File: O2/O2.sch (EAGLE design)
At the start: 29 parts, among them J1 HEAD15-NOSS, J2 HEAD15-NOSS-1, J3 HEAD15-NOSS, J4 HEAD15-NOSS-1, T1 2N2222, T2 2N2222, T3 2N2222

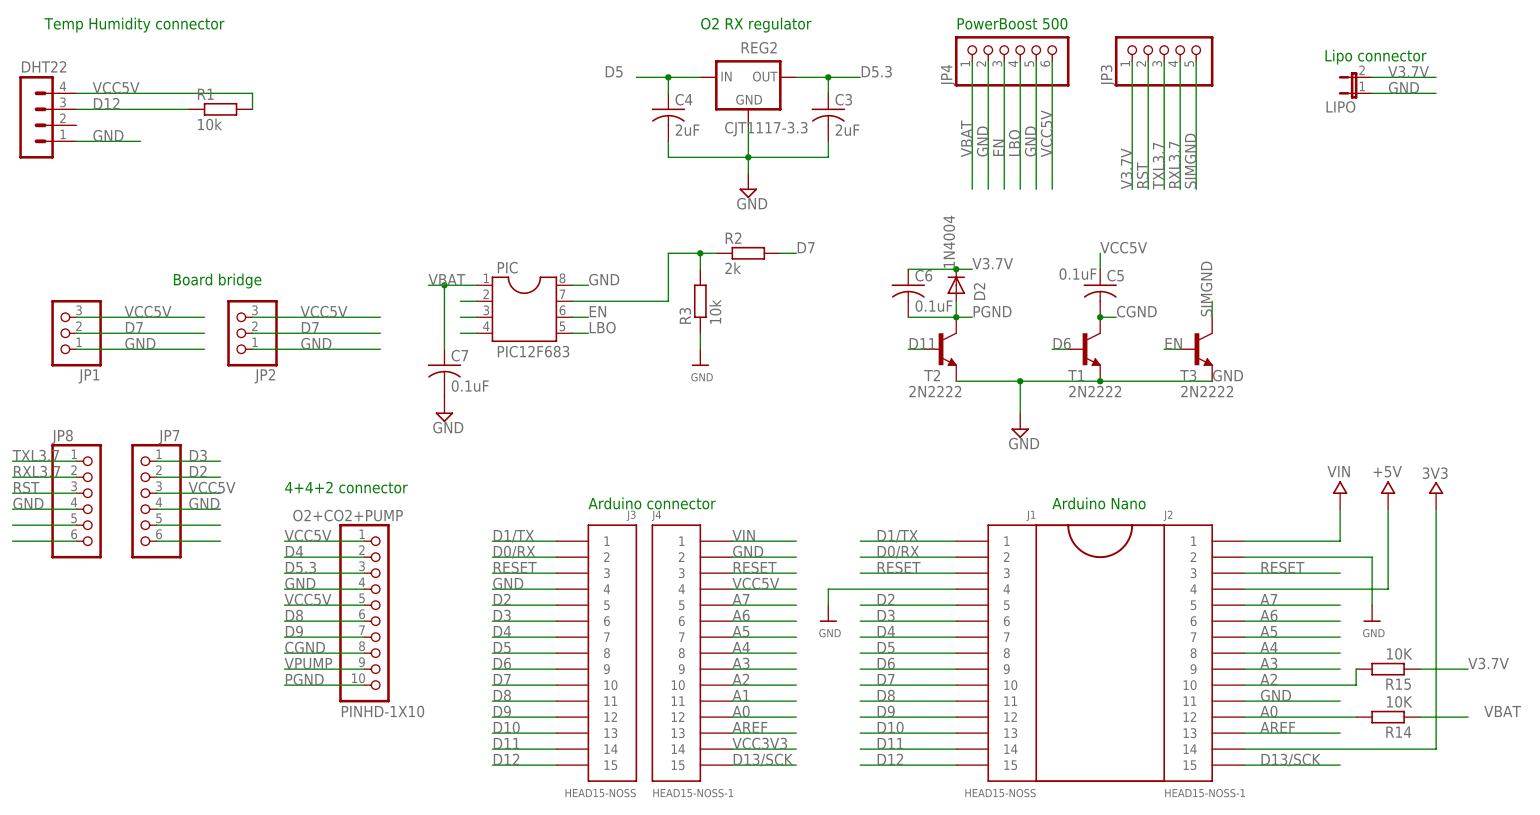
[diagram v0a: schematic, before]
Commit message: Modified the O2 circuits and changed the layout.
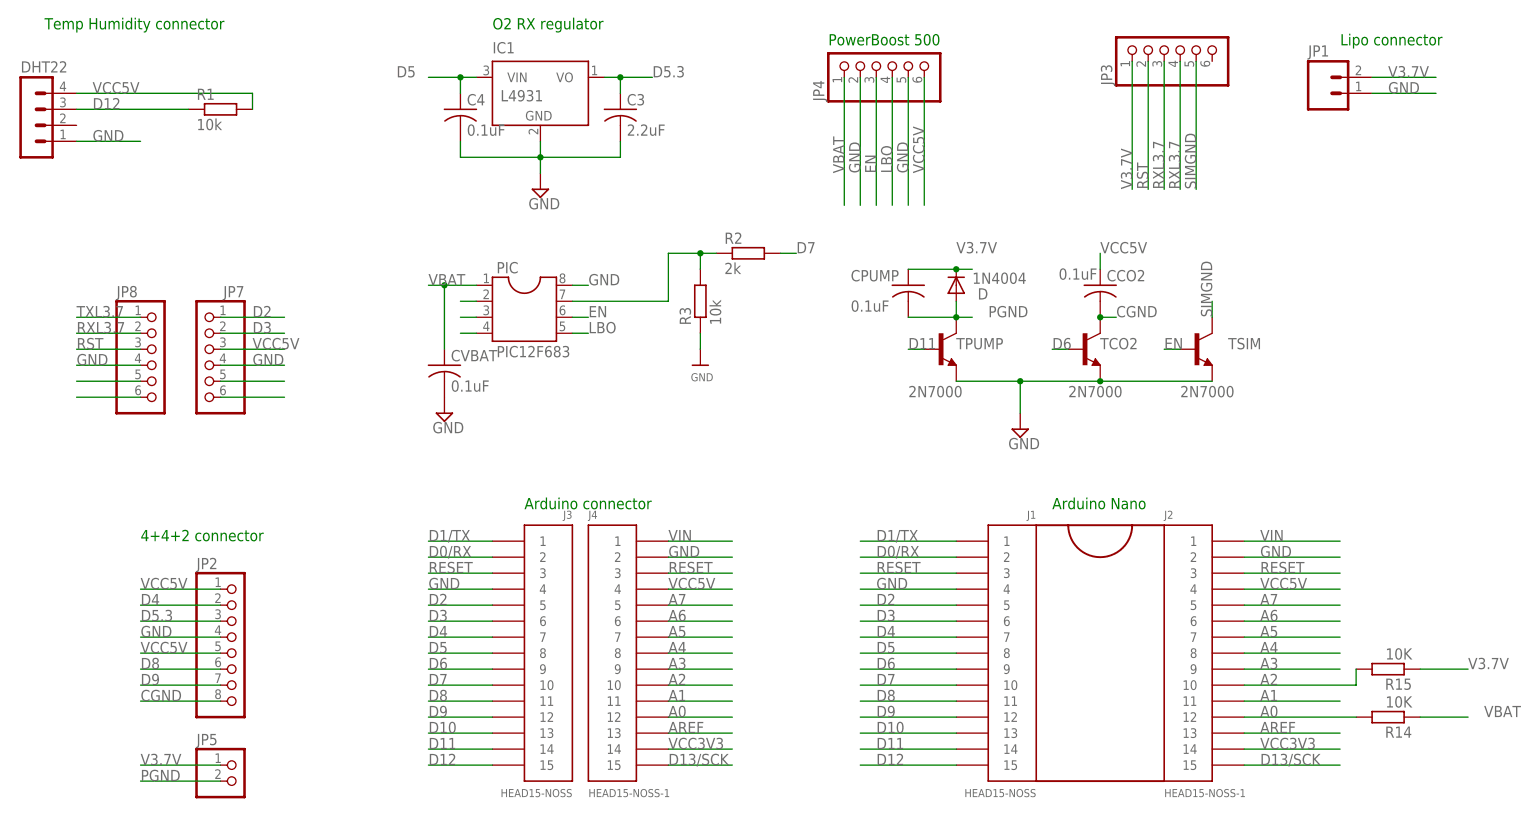
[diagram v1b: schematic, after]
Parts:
- removed LIPO: (no value), jumper:JP1E
- removed O2+CO2+PUMP: PINHD-1X10, adafruit:PINHD-1X10
- removed REG2: CJT1117-3.3, adafruit:MCP1700INLINE
- added IC1: L4931, national-semiconductor:LM2936Z-3.3
- added JP5: (no value), pinhead:PINHD-1X2
- C3: value 2uF -> 2.2uF
- C4: value 2uF -> 0.1uF
- JP1: device adafruit:PINHD-1X3CB -> SparkFun-Connectors:M023.5MM
- JP2: device adafruit:PINHD-1X3CB -> adafruit:PINHD-1X8BIG
- JP3: device pinhead:PINHD-1X55X2MM -> adafruit:PINHD-1X6CB
- TCO2, TPUMP, TSIM: value 2N2222 -> 2N7000
- renumbered C5 to CCO2, C6 to CPUMP, C7 to CVBAT, D2 to D, T1 to TCO2, T2 to TPUMP, T3 to TSIM
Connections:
- removed net VPUMP: O2+CO2+PUMP.9
- net A1: now also J2.11
- net CGND: now also JP2.8; no longer O2+CO2+PUMP.8
- net D11: now also TPUMP.B
- net D2: now also JP7.1; no longer JP7.2
- net D3: now also JP7.2; no longer JP7.1
- net D4: now also JP2.2; no longer O2+CO2+PUMP.2
- net D5: now also IC1.VIN; no longer REG2.IN
- net D5.3: now also IC1.VO, JP2.3; no longer O2+CO2+PUMP.3, REG2.OUT
- net D6: now also TCO2.B
- net D7: no longer JP1.2, JP2.2
- net D8: now also JP2.6; no longer O2+CO2+PUMP.6
- net D9: now also JP2.7; no longer O2+CO2+PUMP.7
- net GND: now also IC1.GND, JP2.4; no longer J2.11, JP2.1, LIPO.1, O2+CO2+PUMP.4, REG2.GND
- net PGND: now also JP5.2; no longer O2+CO2+PUMP.10
- net RXL3.7: now also JP3.3
- net TXL3.7: no longer JP3.3
- net V3.7V: now also JP1.2, JP5.1; no longer LIPO.2
- net VCC5V: now also JP2.1, JP2.5; no longer JP1.3, JP2.3, O2+CO2+PUMP.1, O2+CO2+PUMP.5
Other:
- note removed: "Board bridge"
- moved on the sheet: C3, C4, J3, J4, JP4, JP7, JP8

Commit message: Modified the sch and layout again. Ready for deliver
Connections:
- new net N$4: JP8.6
- net RXL3.7: no longer JP3.4, JP8.6
- net TXL3.7: now also JP3.4
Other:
- note added: "CO2 sensor 4pins"
- note added: "O2 sensor 4pins"
- note added: "Pump 2pins"
- note added: "SIM800L"
- note removed: "4+4+2 connector"
- moved on the sheet: DHT22, JP2, JP4, JP5, R1
